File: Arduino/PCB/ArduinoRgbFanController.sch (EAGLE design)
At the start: 58 parts, among them IC2 ARDUINO_MKRFOX1200PROTOPADS, Q1 IRLML9301TRPBF, Q2 2N7002, Q3 2N7002, Q4 IRLML9301TRPBF

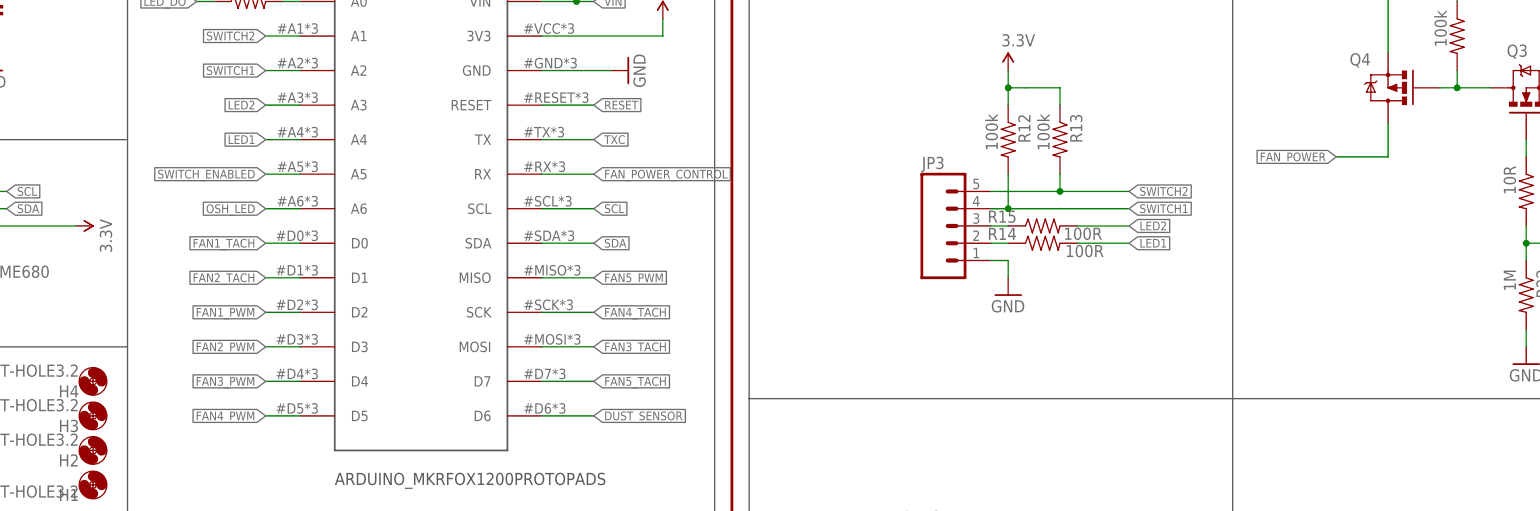
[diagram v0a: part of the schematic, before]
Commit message: Added 12v sense to detect low voltage and supply switched on.
Moved Fan5 connector up to leave a nice space at the bottom for the "Alexa..." thing.
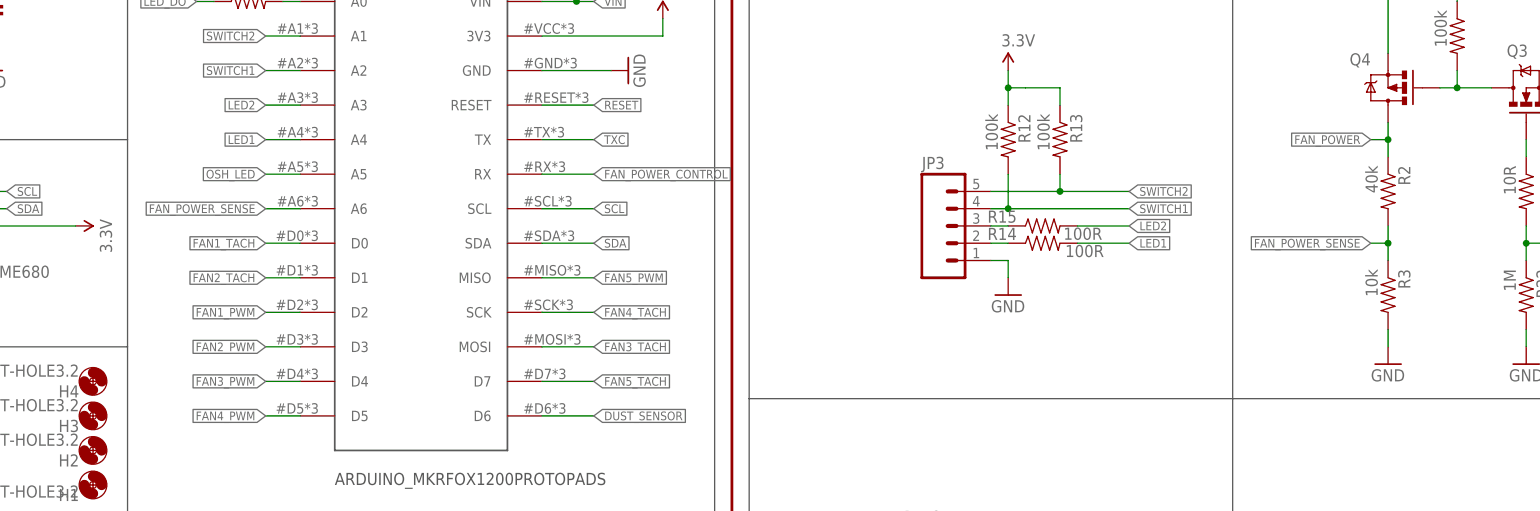
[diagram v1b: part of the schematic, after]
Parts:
- added R2: 40k, SparkFun-Resistors:RESISTOR0805-RES
- added R3: 10k, SparkFun-Resistors:RESISTOR0805-RES
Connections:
- removed net SWITCH_ENABLED: IC2.A5
- new net FAN_POWER_SENSE: IC2.A6, R2.2, R3.1
- net FAN_POWER: now also R2.1
- net GND: now also R3.2
- net OSH_LED: now also IC2.A5; no longer IC2.A6
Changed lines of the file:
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@@
 <part name="SUPPLY2" library="SparkFun-Aesthetics" deviceset="VIN" device=""/>
 <part name="GND6" library="SparkFun-Aesthetics" deviceset="GND" device=""/>
+<part name="R2" library="SparkFun-Resistors" deviceset="RESISTOR" device="0805-RES" value="40k"/>
+<part name="R3" library="SparkFun-Resistors" deviceset="RESISTOR" device="0805-RES" value="10k"/>
+<part name="GND7" library="SparkFun-Aesthetics" deviceset="GND" device=""/>
 </parts>
 <sheets>
@@
 <instance part="SUPPLY2" gate="G$1" x="264.16" y="83.82"/>
 <instance part="GND6" gate="1" x="264.16" y="73.66"/>
+<instance part="R2" gate="G$1" x="345.44" y="139.7" smashed="yes" rot="R270">
+<attribute name="NAME" x="346.9386" y="143.51" size="1.778" layer="95" rot="R270"/>
+<attribute name="VALUE" x="342.138" y="143.51" size="1.778" layer="96" rot="R270"/>
+</instance>
+<instance part="R3" gate="G$1" x="345.44" y="124.46" smashed="yes" rot="R270">
+<attribute name="NAME" x="346.9386" y="128.27" size="1.778" layer="95" rot="R270"/>
+<attribute name="VALUE" x="342.138" y="128.27" size="1.778" layer="96" rot="R270"/>
+</instance>
+<instance part="GND7" gate="1" x="345.44" y="114.3"/>
 </instances>
 <busses>
@@
 <pinref part="GND6" gate="1" pin="GND"/>
 </segment>
+<segment>
+<pinref part="GND7" gate="1" pin="GND"/>
+<pinref part="R3" gate="G$1" pin="2"/>
+<wire x1="345.44" y1="116.84" x2="345.44" y2="119.38" width="0.1524" layer="91"/>
+</segment>
 </net>
 <net name="12V" class="0">
@@
 </segment>
 <segment>
-<pinref part="IC2" gate="G$1" pin="A6"/>
-<wire x1="185.42" y1="137.16" x2="180.34" y2="137.16" width="0.1524" layer="91"/>
-<label x="180.34" y="137.16" size="1.27" layer="95" rot="R180" xref="yes"/>
+<pinref part="IC2" gate="G$1" pin="A5"/>
+<wire x1="185.42" y1="142.24" x2="180.34" y2="142.24" width="0.1524" layer="91"/>
+<label x="180.34" y="142.24" size="1.27" layer="95" rot="R180" xref="yes"/>
 </segment>
 </net>
@@
 <segment>
 <pinref part="Q4" gate="G$1" pin="D"/>
-<wire x1="345.44" y1="149.86" x2="345.44" y2="144.78" width="0.1524" layer="91"/>
-<wire x1="345.44" y1="144.78" x2="337.82" y2="144.78" width="0.1524" layer="91"/>
-<label x="337.82" y="144.78" size="1.27" layer="95" rot="R180" xref="yes"/>
+<wire x1="345.44" y1="149.86" x2="345.44" y2="147.32" width="0.1524" layer="91"/>
+<wire x1="345.44" y1="147.32" x2="342.9" y2="147.32" width="0.1524" layer="91"/>
+<label x="342.9" y="147.32" size="1.27" layer="95" rot="R180" xref="yes"/>
+<pinref part="R2" gate="G$1" pin="1"/>
+<wire x1="345.44" y1="144.78" x2="345.44" y2="147.32" width="0.1524" layer="91"/>
+<junction x="345.44" y="147.32"/>
 </segment>
 <segment>
@@
 </segment>
 </net>
-<net name="SWITCH_ENABLED" class="0">
-<segment>
-<pinref part="IC2" gate="G$1" pin="A5"/>
-<wire x1="185.42" y1="142.24" x2="180.34" y2="142.24" width="0.1524" layer="91"/>
-<label x="180.34" y="142.24" size="1.27" layer="95" rot="R180" xref="yes"/>
-</segment>
-</net>
+<net name="FAN_POWER_SENSE" class="0">
+<segment>
+<pinref part="IC2" gate="G$1" pin="A6"/>
+<wire x1="185.42" y1="137.16" x2="180.34" y2="137.16" width="0.1524" layer="91"/>
+<label x="180.34" y="137.16" size="1.27" layer="95" rot="R180" xref="yes"/>
+</segment>
+<segment>
+<pinref part="R2" gate="G$1" pin="2"/>
+<pinref part="R3" gate="G$1" pin="1"/>
+<wire x1="345.44" y1="129.54" x2="345.44" y2="132.08" width="0.1524" layer="91"/>
+<wire x1="345.44" y1="132.08" x2="345.44" y2="134.62" width="0.1524" layer="91"/>
+<wire x1="345.44" y1="132.08" x2="342.9" y2="132.08" width="0.1524" layer="91"/>
+<label x="342.9" y="132.08" size="1.27" layer="95" rot="R180" xref="yes"/>
+<junction x="345.44" y="132.08"/>
+</segment>
+</net>

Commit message: Tidied up
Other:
- note added: "No Int."
- note added: "No Pwm"
- note added: "int"
- note added: "pwm"
- moved on the sheet: C7, D2, H1, H2, H3, H4, JP13, JP6, JP8, JP9, Q3, Q4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

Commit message: Added some value for components and some notes and dimensions for the PCB.
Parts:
- C5: FARNELL (none) -> 1135048
- R11: value (none) -> 470R
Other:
- note added: "C5: Ideally 1000uF @ 6.3V, Farnell 1135048 100uF Tant"
- note added: "Notes: * Use a bigger fet for main 12v switch. Some 12V fans can run at 5A. * Include PolyFuse on main fan supply pre FET. * Fan 5 should be taken from 12v not Fan supply so it can be run without the other fans having power (PWM Fans run even on zero PWM). * Second switching control so Fans 1/2 and 3/4 have master fet switches. * Reverse mount vertical USB socket options (switched) for air freshn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"
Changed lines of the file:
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@@
 <part name="GND28" library="SparkFun-Aesthetics" deviceset="GND" device=""/>
 <part name="SUPPLY10" library="SparkFun-Aesthetics" deviceset="VIN" device=""/>
-<part name="R11" library="SparkFun-Resistors" deviceset="RESISTOR" device="0805-RES"/>
+<part name="R11" library="SparkFun-Resistors" deviceset="RESISTOR" device="0805-RES" value="470R"/>
 <part name="C4" library="SparkFun-Capacitors" deviceset="47UF-10V-10%(TANT)" device="" value="47uF"/>
-<part name="C5" library="SparkFun-Capacitors" deviceset="47UF-10V-10%(TANT)" device="" value="47uF"/>
+<part name="C5" library="SparkFun-Capacitors" deviceset="47UF-10V-10%(TANT)" device="" value="47uF">
+<attribute name="FARNELL" value="1135048"/>
+</part>
 <part name="GND10" library="SparkFun-Aesthetics" deviceset="GND" device=""/>
 <part name="GND13" library="SparkFun-Aesthetics" deviceset="GND" device=""/>
@@
 <wire x1="187.96" y1="60.96" x2="187.96" y2="38.1" width="0.1524" layer="97"/>
 <wire x1="144.78" y1="60.96" x2="129.54" y2="60.96" width="0.1524" layer="97"/>
+<text x="252.222" y="3.302" size="1.778" layer="97">Notes:
+* Use a bigger fet for main 12v switch. Some 12V fans can run at 5A.
+* Include PolyFuse on main fan supply pre FET.
+* Fan 5 should be taken from 12v not Fan supply so it can be run without the other fans having power (PWM Fans run even on zero PWM).
+* Second switching control so Fans 1/2 and 3/4 have master fet switches.
+* Reverse mount vertical USB socket options (switched) for air freshner
+* Forward mount vertical USB socket for phone charge?
+* Can Fans 1 &amp; 2, 3 &amp; 4 share pwm signals?</text>
+<text x="33.02" y="48.26" size="1.778" layer="97">C5: Ideally 1000uF @ 6.3V, Farnell 1135048 100uF Tant</text>
 </plain>
 <instances>
@@
 <attribute name="NAME" x="24.638" y="44.323" size="1.778" layer="95"/>
 <attribute name="VALUE" x="28.956" y="37.211" size="1.778" layer="96" rot="R180"/>
+<attribute name="FARNELL" x="25.4" y="40.64" size="1.778" layer="96" rot="R90" display="off"/>
 </instance>
 <instance part="GND10" gate="1" x="35.56" y="40.64" rot="R90"/>
